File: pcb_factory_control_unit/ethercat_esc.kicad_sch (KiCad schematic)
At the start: 68 parts, among them U16 24LC512, Y2 25MHz

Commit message: Changed LED ReverseMount Footprint, Removed PullUp, HSOS Logo
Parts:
- D6, D7: footprint liebler_OPTO:LED_1206_3216Metric_ReverseMount -> LED_SMD:LED_1206_3216Metric_ReverseMount_Hole1.8x2.4mm

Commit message: PCB Control Unit: add EEPROM-select jumpers on EtherCAT ESC, new J7 connector
ethercat_esc.kicad_sch: add EESDA solder jumpers JP4/JP5 with pull-up
resistor R89 (3k3) and a RUNLED_PU label, wired to GND/+3V3.
conn.kicad_sch: add 4-pin connector J7 (+12V/GND).
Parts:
- added JP4, JP5: EESDA, symbol Jumper:SolderJumper_3_Bridged12
- added R89: 3k3, Resistor_SMD:R_0402_1005Metric, symbol Device:R
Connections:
- net +3V3: no longer R78.1
- net EESDA: now also JP4.2 (C); no longer R83.2
- net GND: now also R89.1
- new net: JP4.3 (B), R89.2
- new net: JP4.1 (A), R83.2
- new net RUNLED_PU: R78.1

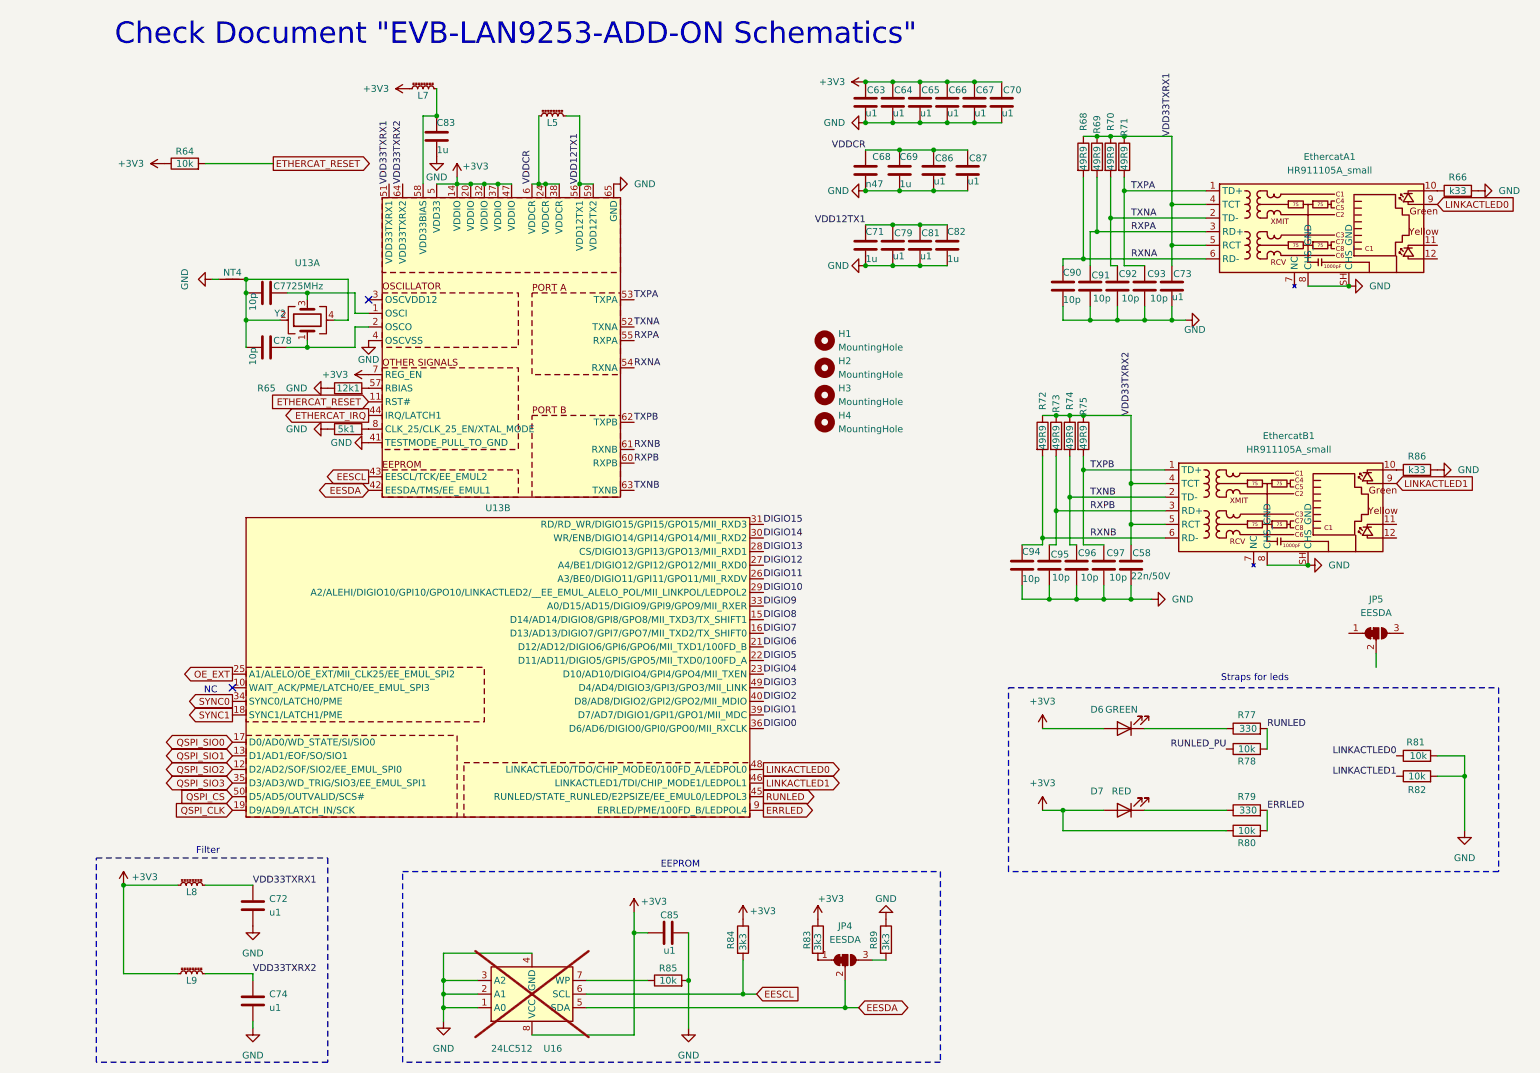
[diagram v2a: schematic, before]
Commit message: Improved Schematics EtherCAT after Claude-Session. Refactoring in Builder
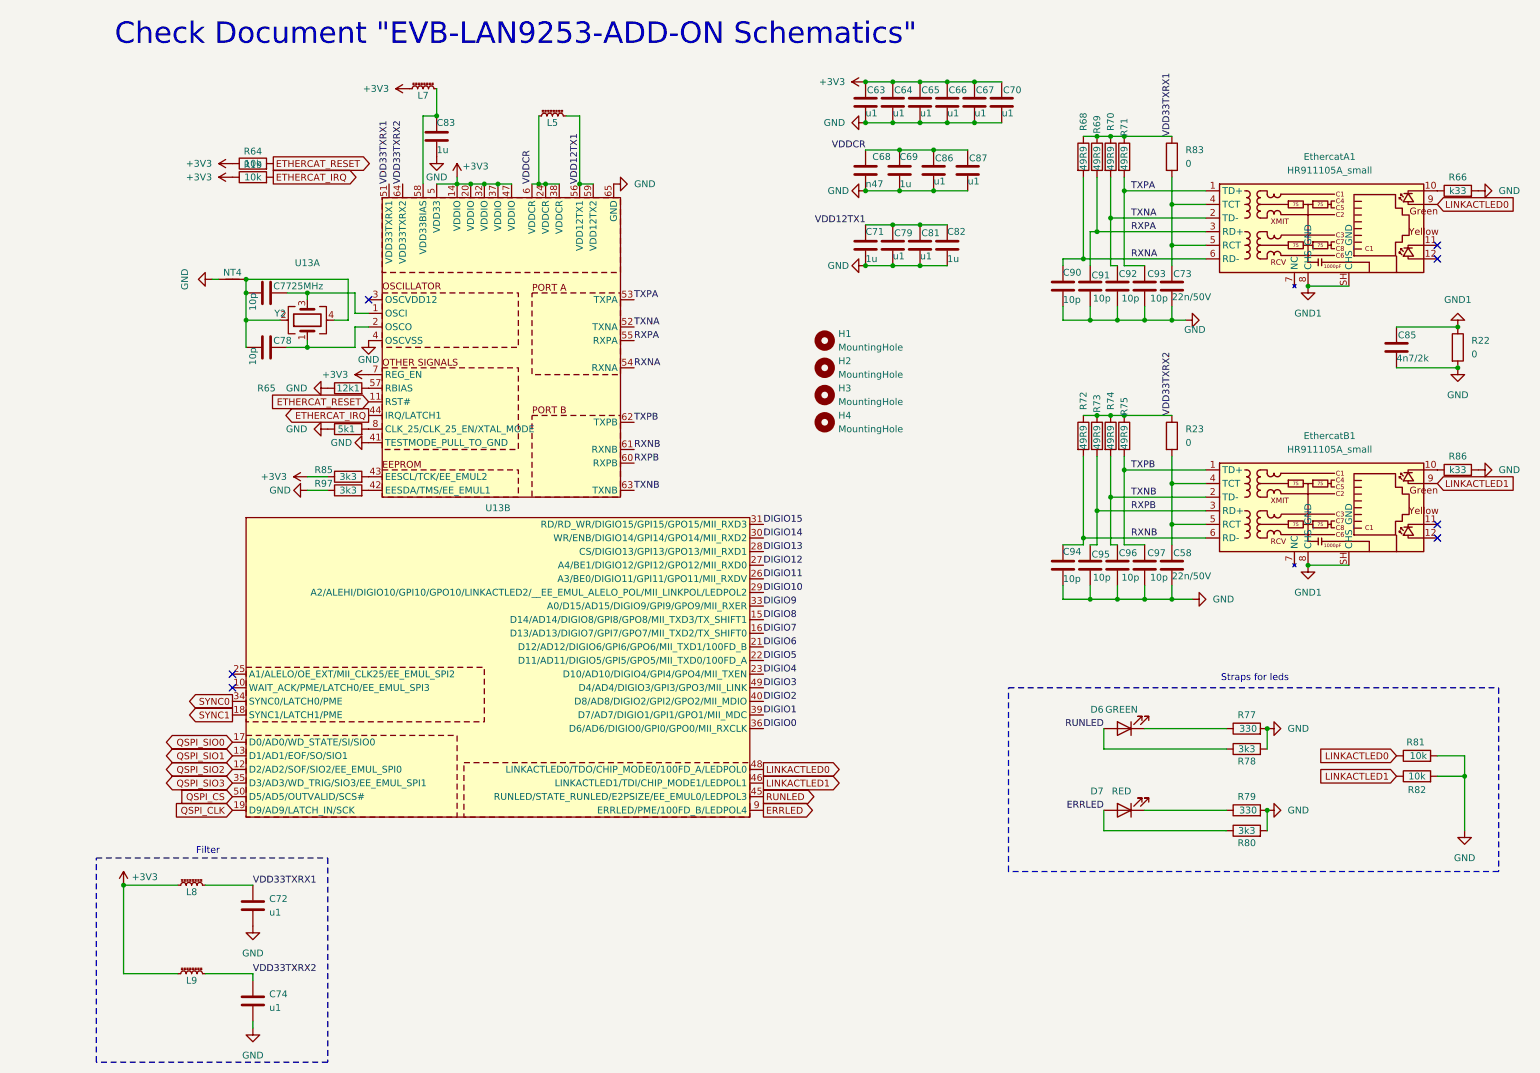
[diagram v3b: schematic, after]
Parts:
- removed JP4, JP5: EESDA, symbol Jumper:SolderJumper_3_Bridged12
- removed R84, R89: 3k3, Resistor_SMD:R_0402_1005Metric, symbol Device:R
- removed U16: 24LC512, Package_DIP:DIP-8_W7.62mm_Socket_LongPads, symbol Memory_EEPROM:24LC512
- added R19: 10k, Resistor_SMD:R_0402_1005Metric, symbol Device:R
- added R22, R23: 0, Resistor_SMD:R_0805_2012Metric_Pad1.20x1.40mm_HandSolder, symbol Device:R
- added R97: 3k3, Resistor_SMD:R_0402_1005Metric, symbol Device:R
- C73: value u1 -> 22n/50V
- C85: value u1 -> 4n7/2k; footprint Capacitor_SMD:C_0402_1005Metric -> Capacitor_SMD:C_0805_2012Metric_Pad1.18x1.45mm_HandSolder
- R78, R80, R85: value 10k -> 3k3
- R83: value 3k3 -> 0; footprint Resistor_SMD:R_0402_1005Metric -> Resistor_SMD:R_0805_2012Metric_Pad1.20x1.40mm_HandSolder
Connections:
- net RUNLED_PU is gone; now on net RUNLED: R78.1
- net +3V3: now also R85.1, R19.1; no longer C85.1, D6.2 (A), D7.2 (A), R80.1, R83.1
- net ERRLED: now also D7.2 (A), R80.1; no longer R79.2, R80.2
- net ETHERCAT_IRQ: now also R19.2
- net GND: now also R77.2, R78.2, R79.2, R80.2, R22.2, R97.1; no longer EthercatA1.8 (CHS_GND), EthercatA1.SH (CHS_GND), EthercatB1.8 (CHS_GND), EthercatB1.SH (CHS_GND), R85.2
- net RUNLED: now also D6.2 (A); no longer R77.2, R78.2
- net VDD33TXRX1: now also R83.1; no longer C73.1, EthercatA1.4 (TCT), EthercatA1.5 (RCT)
- net VDD33TXRX2: now also R23.1; no longer C58.1, EthercatB1.4 (TCT), EthercatB1.5 (RCT)
- net at R83.2: now also C73.1, EthercatA1.4 (TCT), EthercatA1.5 (RCT)
- net EESCL: no longer names the net of U13.43 (EESCL/TCK/EE_EMUL2)
- net EESCL: now also R85.2
- net EESDA: no longer names the net of U13.42 (EESDA/TMS/EE_EMUL1)
- net EESDA: now also R97.2
- net OE_EXT: no longer names the net of U13.25 (A1/ALELO/OE_EXT/MII_CLK25/EE_EMUL_SPI2)
- new net: C58.1, EthercatB1.4 (TCT), EthercatB1.5 (RCT), R23.2
- new net GND1: C85.1, EthercatA1.8 (CHS_GND), EthercatA1.SH (CHS_GND), EthercatB1.8 (CHS_GND), EthercatB1.SH (CHS_GND), R22.1
- no-connect marks 2 -> 7
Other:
- note removed: "EEPROM"
- note removed: "NC"
- moved on the sheet: C58, C94, C95, C96, C97, EthercatB1, R64, R72, R73, R74, R75, R86

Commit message: Control Unit PCB: schematic rework (PSU, MX26631DL, XL6009 module, ERC fixes), new placement on 90 mm high board
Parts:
- renumbered C58 to C100, C85 to C101, C74 to C73, C77 to C74, C78 to C75, C83 to C76, C63 to C77, C68 to C78, C71 to C79, C64 to C80, C79 to C81, C69 to C82, C65 to C83, C81 to C84, C86 to C85, C66 to C86, C82 to C87, C87 to C88, C67 to C89, C70 to C90, C90 to C91, C94 to C92, C91 to C93, C95 to C94, C92 to C95, C93 to C97, C97 to C98, C73 to C99, D6 to D16, D7 to D17, L7 to L10, L5 to L11, NT4 to NT3, R80 to R100, R81 to R101, R82 to R102, R66 to R103, R22 to R104, R86 to R105, R64 to R81, R19 to R82, R65 to R83, R67 to R84, R97 to R86, R68 to R87, R72 to R88, R69 to R89, R73 to R90, R70 to R91, R74 to R92, R71 to R93, R75 to R94, R83 to R95, R23 to R96, R77 to R97, R78 to R98, R79 to R99
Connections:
- no-connect marks 7 -> 23

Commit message: FCB ready for review
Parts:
- added H5: MountingHole, liebler_DRAWINGS:barrel_jack_positive_polarity, symbol Mechanical:MountingHole
- D16: value GREEN -> EtherCat RUN
- D17: value RED -> EtherCAT ERR
- R104: value 0 -> GND_ETH
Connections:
- net CLK_GND: now reaches C74.2, C75.2, NT3.2, Y2.2 (G), Y2.4 (G)
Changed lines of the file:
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@@
 		)
 	)
+	(label "CLK_GND"
+		(at 45.72 50.8 0)
+		(effects
+			(font
+				(size 1.27 1.27)
+			)
+			(justify left bottom)
+		)
+	)
 	(global_label "ERRLED"
 		(shape output)
@@
 	)
 	(symbol
+		(lib_id "Mechanical:MountingHole")
+		(at 153.67 83.82 0)
+		(unit 1)
+		(body_style 1)
+		(exclude_from_sim no)
+		(in_bom no)
+		(on_board yes)
+		(in_pos_files yes)
+		(dnp no)
+		(fields_autoplaced yes)
+		(property "Reference" "H5"
+			(at 156.21 82.5499 0)
+			(show_name no)
+			(do_not_autoplace no)
+			(effects
+				(font
+					(size 1.27 1.27)
+				)
+				(justify left)
+			)
+		)
+		(property "Value" "MountingHole"
+			(at 156.21 85.0899 0)
+			(show_name no)
+			(do_not_autoplace no)
+			(effects
+				(font
+					(size 1.27 1.27)
+				)
+				(justify left)
+			)
+		)
+		(property "Footprint" "liebler_DRAWINGS:barrel_jack_positive_polarity"
+			(at 153.67 83.82 0)
+			(hide yes)
+			(show_name no)
+			(do_not_autoplace no)
+			(effects
+				(font
+					(size 1.27 1.27)
+				)
+			)
+		)
+		(property "Datasheet" ""
+			(at 153.67 83.82 0)
+			(hide yes)
+			(show_name no)
+			(do_not_autoplace no)
+			(effects
+				(font
+					(size 1.27 1.27)
+				)
+			)
+		)
+		(property "Description" "Mounting Hole without connection"
+			(at 153.67 83.82 0)
+			(hide yes)
+			(show_name no)
+			(do_not_autoplace no)
+			(effects
+				(font
+					(size 1.27 1.27)
+				)
+			)
+		)
+		(instances
+			(project "pcb_factory_control_unit"
+				(path "/9c57264a-0988-4c94-95c0-340e4ca73bd5/f2fdf4e4-4878-452d-8edd-af4cbe9f58a2"
+					(reference "H5")
+					(unit 1)
+				)
+			)
+		)
+	)
+	(symbol
 		(lib_id "Device:C")
 		(at 260.35 63.5 0)
@@
 			)
 		)
-		(property "Value" "0"
+		(property "Value" "GND_ETH"
 			(at 274.32 64.7699 0)
 			(show_name no)
@@
 			)
 		)
-		(property "Value" "RED"
+		(property "Value" "EtherCAT ERR"
 			(at 209.042 146.304 0)
 			(show_name no)
@@
 			)
 		)
-		(property "Value" "GREEN"
+		(property "Value" "EtherCat RUN"
 			(at 209.042 131.064 0)
 			(show_name no)
